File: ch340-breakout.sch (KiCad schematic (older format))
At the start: 19 parts, among them J1 USB_B_Mini, J2 Conn_01x08_Male, J3 Conn_02x05_Odd_Even, U1 SPX3819M5-L-3-3, U2 USBLC6-2SC6, U3 CH340G, Y1 12Mhz

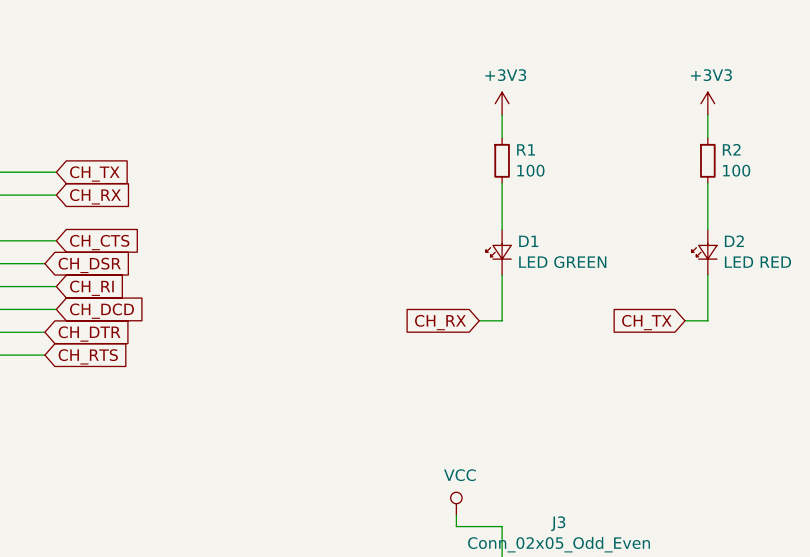
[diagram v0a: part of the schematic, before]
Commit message: finalizing and add power on led
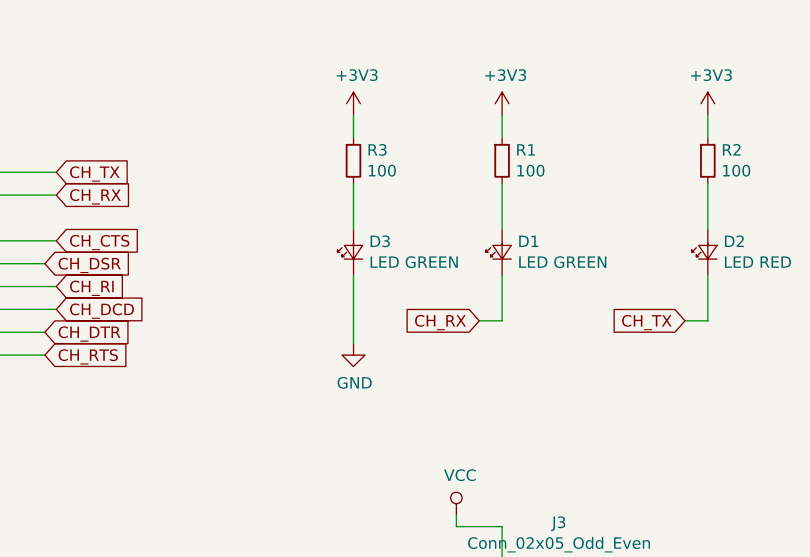
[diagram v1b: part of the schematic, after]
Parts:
- added D3: LED GREEN, LED_SMD:LED_0805_2012Metric, symbol Device:LED_Small
- added R3: 100, Resistor_SMD:R_0805_2012Metric, symbol Device:R_Small
- C4, C6: footprint Capacitor_SMD:C_0805_2012Metric_Pad1.15x1.40mm_HandSolder -> Capacitor_SMD:C_0805_2012Metric
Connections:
- net +3V3: now also R3.1
- net GND: now also D3.1 (K)
- new net: D3.2 (A), R3.2
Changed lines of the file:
@@
 F 0 "C4" H 4642 3646 50  0000 L CNN
 F 1 "22p" H 4642 3555 50  0000 L CNN
-F 2 "Capacitor_SMD:C_0805_2012Metric_Pad1.15x1.40mm_HandSolder" H 4550 3600 50  0001 C CNN
+F 2 "Capacitor_SMD:C_0805_2012Metric" H 4550 3600 50  0001 C CNN
 F 3 "~" H 4550 3600 50  0001 C CNN
 	1    4550 3600
@@
 F 0 "C6" H 5192 3646 50  0000 L CNN
 F 1 "22p" H 5192 3555 50  0000 L CNN
-F 2 "Capacitor_SMD:C_0805_2012Metric_Pad1.15x1.40mm_HandSolder" H 5100 3600 50  0001 C CNN
+F 2 "Capacitor_SMD:C_0805_2012Metric" H 5100 3600 50  0001 C CNN
 F 3 "~" H 5100 3600 50  0001 C CNN
 	1    5100 3600
@@
 Wire Wire Line
 	2600 5800 2650 5800
+$Comp
+L Device:LED_Small D3
+U 1 1 5E0684E1
+P 7700 2900
+F 0 "D3" V 7746 2832 50  0000 R CNN
+F 1 "LED GREEN" V 7655 2832 50  0000 R CNN
+F 2 "LED_SMD:LED_0805_2012Metric" V 7700 2900 50  0001 C CNN
+F 3 "~" V 7700 2900 50  0001 C CNN
+	1    7700 2900
+	0    -1   -1   0
+$EndComp
+$Comp
+L Device:R_Small R3
+U 1 1 5E0684EB
+P 7700 2500
+F 0 "R3" H 7759 2546 50  0000 L CNN
+F 1 "100" H 7759 2455 50  0000 L CNN
+F 2 "Resistor_SMD:R_0805_2012Metric" H 7700 2500 50  0001 C CNN
+F 3 "~" H 7700 2500 50  0001 C CNN
+	1    7700 2500
+	1    0    0    -1
+$EndComp
+Wire Wire Line
+	7700 2800 7700 2600
+$Comp
+L power:+3V3 #PWR024
+U 1 1 5E0684F6
+P 7700 2300
+F 0 "#PWR024" H 7700 2150 50  0001 C CNN
+F 1 "+3V3" H 7715 2473 50  0000 C CNN
+F 2 "" H 7700 2300 50  0001 C CNN
+F 3 "" H 7700 2300 50  0001 C CNN
+	1    7700 2300
+	1    0    0    -1
+$EndComp
+Wire Wire Line
+	7700 2300 7700 2400
+$Comp
+L power:GND #PWR025
+U 1 1 5E0759C3
+P 7700 3300
+F 0 "#PWR025" H 7700 3050 50  0001 C CNN
+F 1 "GND" H 7705 3127 50  0000 C CNN
+F 2 "" H 7700 3300 50  0001 C CNN
+F 3 "" H 7700 3300 50  0001 C CNN
+	1    7700 3300
+	1    0    0    -1
+$EndComp
+Wire Wire Line
+	7700 3000 7700 3300
 $EndSCHEMATC

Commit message: prepare for publishing: fixing LED resistor values, archive footprints, add missing data sheets
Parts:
- C1, C2, C3, C4, C5, C6: footprint Capacitor_SMD:C_0805_2012Metric -> ch340-breakout:C_0805_2012Metric
- D1, D2, D3: footprint LED_SMD:LED_0805_2012Metric -> ch340-breakout:LED_0805_2012Metric
- F1: footprint Fuse:Fuse_0805_2012Metric -> ch340-breakout:Fuse_0805_2012Metric
- J1: footprint Connector_USB:USB_Mini-B_Lumberg_2486_01_Horizontal -> ch340-breakout:USB_Mini-B_Lumberg_2486_01_Horizontal
- J2: footprint Connector_PinHeader_2.54mm:PinHeader_1x08_P2.54mm_Vertical -> ch340-breakout:PinHeader_1x08_P2.54mm_Vertical
- J3: footprint Connector_PinHeader_2.54mm:PinHeader_2x05_P2.54mm_Vertical -> ch340-breakout:PinHeader_2x05_P2.54mm_Vertical
- JP1: footprint Connector_PinHeader_2.54mm:PinHeader_1x03_P2.54mm_Vertical -> ch340-breakout:PinHeader_1x03_P2.54mm_Vertical
- R1, R3: value 100 -> 3K3; footprint Resistor_SMD:R_0805_2012Metric -> ch340-breakout:R_0805_2012Metric
- R2: value 100 -> 2K2; footprint Resistor_SMD:R_0805_2012Metric -> ch340-breakout:R_0805_2012Metric
- U1: footprint Package_TO_SOT_SMD:SOT-23-5 -> ch340-breakout:SOT-23-5
- U2: footprint Package_TO_SOT_SMD:SOT-23-6 -> ch340-breakout:SOT-23-6
- U3: footprint Package_SO:SOIC-16_3.9x9.9mm_P1.27mm -> ch340-breakout:SOIC-16_3.9x9.9mm_P1.27mm
- Y1: footprint Crystal:Crystal_SMD_HC49-SD -> ch340-breakout:Crystal_SMD_HC49-SD
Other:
- note added: "CH340-breakout"
- note added: "https://820labs.net/projects/ch340-breakout"
- moved on the sheet: C1, C2, C3, C4, C5, C6, D1, D2, D3, F1, J1, J2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
